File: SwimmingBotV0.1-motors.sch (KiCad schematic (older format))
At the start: 40 parts, among them P6 FIN1, P7 FIN2, P8 MOT1, P9 MOT2, Q10 PMV45EN2, Q11 PMV45EN2, Q12 PMV45EN2, Q13 PMV45EN2, Q14 PMV45EN2, Q15 PMV45EN2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

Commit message: woohoo getting there
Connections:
- net A1: now also P8.3 (P3); no longer P8.1 (P1)
- net A2: now also P9.3 (P3); no longer P9.1 (P1)
- net C1: now also P8.1 (P1); no longer P8.3 (P3)
- net C2: now also P9.1 (P1); no longer P9.3 (P3)
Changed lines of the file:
@@
 $Descr A4 11693 8268
 encoding utf-8
-Sheet 6 8
+Sheet 4 8
 Title ""
 Date ""
@@
 Wire Wire Line
 	8600 1500 8400 1500
-Text Label 8400 750  0    60   ~ 0
+Text Label 8400 950  0    60   ~ 0
 A1
 Text Label 8400 850  0    60   ~ 0
 B1
-Text Label 8400 950  0    60   ~ 0
+Text Label 8400 750  0    60   ~ 0
 C1
-Text Label 8400 1500 0    60   ~ 0
+Text Label 8400 1300 0    60   ~ 0
 C2
 Text Label 8400 1400 0    60   ~ 0
 B2
-Text Label 8400 1300 0    60   ~ 0
+Text Label 8400 1500 0    60   ~ 0
 A2
 Text Label 7100 5400 1    60   ~ 0

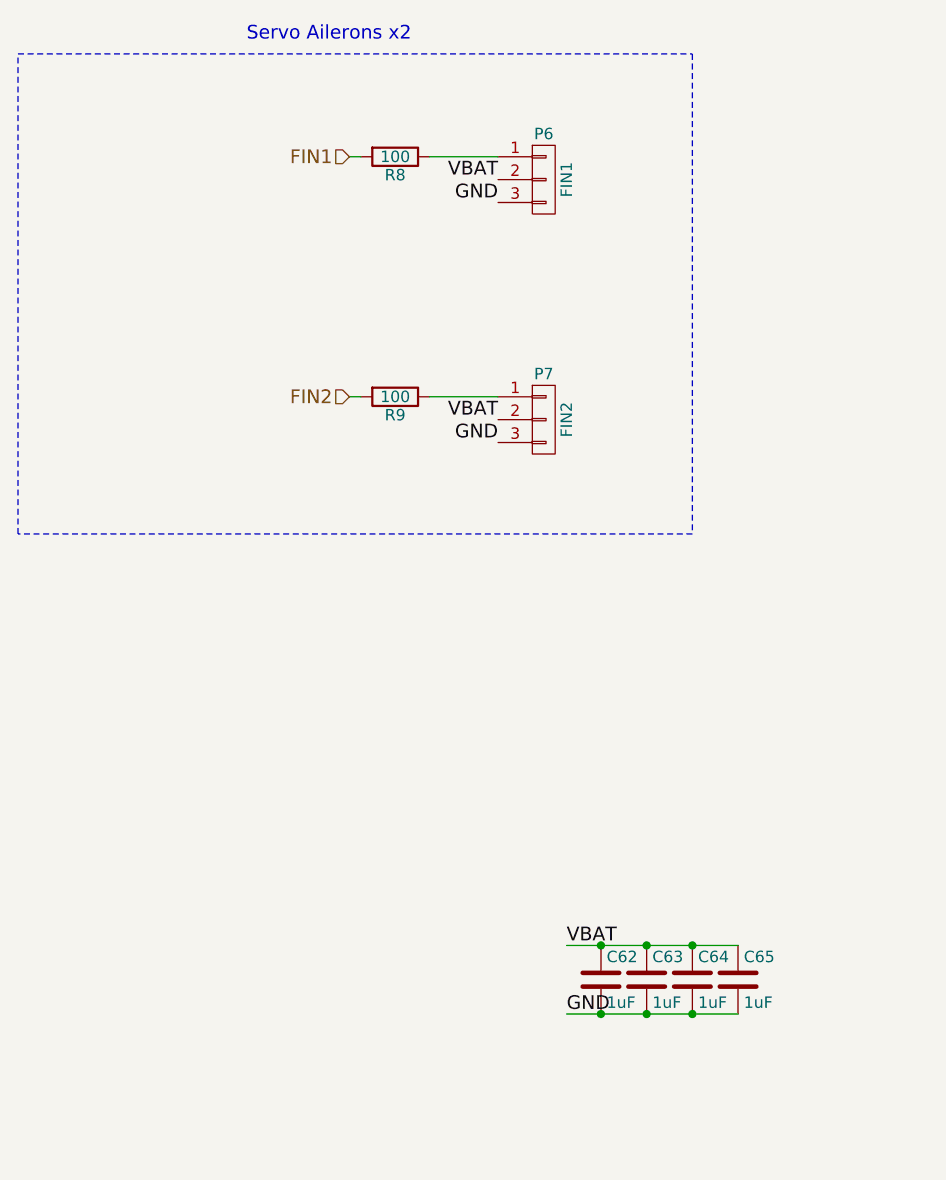
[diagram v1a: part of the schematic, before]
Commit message: potentially done with parts removal and reselection, on to pcb layout
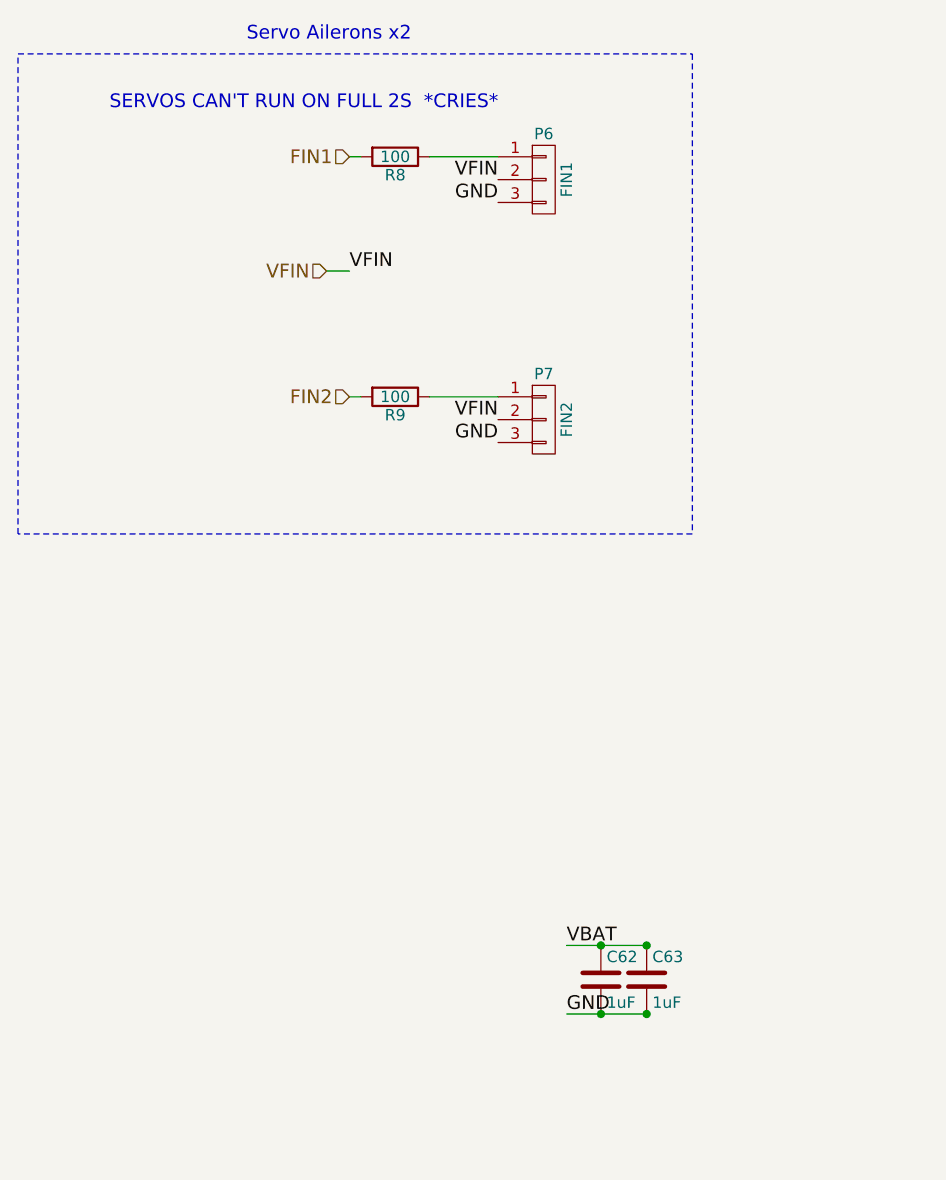
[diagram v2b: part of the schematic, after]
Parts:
- removed C64, C65: 1uF, Capacitors_SMD:C_0402, symbol C
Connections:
- net VBAT: no longer P6.2 (P2), P7.2 (P2)
- new net VFIN: P6.2 (P2), P7.2 (P2)
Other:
- note added: "SERVOS CAN'T RUN ON FULL 2S *CRIES*"
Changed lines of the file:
@@
 Wire Notes Line
 	750  2800 750  700
-Text Label 2850 1250 2    60   ~ 0
-VBAT
 Text Label 2850 2300 2    60   ~ 0
-VBAT
+VFIN
 Text Label 2850 1350 2    60   ~ 0
 GND
@@
 	1    0    0    -1
 $EndComp
-$Comp
-L C C64
-U 1 1 574E8796
-P 3700 4750
-F 0 "C64" H 3725 4850 50  0000 L CNN
-F 1 "1uF" H 3725 4650 50  0000 L CNN
-F 2 "Capacitors_SMD:C_0402" H 3738 4600 50  0001 C CNN
-F 3 "" H 3700 4750 50  0000 C CNN
-	1    3700 4750
-	1    0    0    -1
-$EndComp
-$Comp
-L C C65
-U 1 1 574E881F
-P 3900 4750
-F 0 "C65" H 3925 4850 50  0000 L CNN
-F 1 "1uF" H 3925 4650 50  0000 L CNN
-F 2 "Capacitors_SMD:C_0402" H 3938 4600 50  0001 C CNN
-F 3 "" H 3900 4750 50  0000 C CNN
-	1    3900 4750
-	1    0    0    -1
-$EndComp
-Wire Wire Line
-	3150 4600 3900 4600
-Connection ~ 3700 4600
 Connection ~ 3500 4600
-Wire Wire Line
-	3150 4900 3900 4900
 Connection ~ 3500 4900
-Connection ~ 3700 4900
 Connection ~ 3300 4600
 Connection ~ 3300 4900
@@
 Text Label 3150 4900 0    60   ~ 0
 GND
+Text Notes 1150 950  0    60   ~ 0
+SERVOS CAN'T RUN ON FULL 2S  *CRIES*
+Text Label 2850 1250 2    60   ~ 0
+VFIN
+Text HLabel 2100 1650 0    60   Input ~ 0
+VFIN
+Wire Wire Line
+	2100 1650 2200 1650
+Text Label 2200 1650 0    60   ~ 0
+VFIN
+Wire Wire Line
+	3150 4600 3500 4600
+Wire Wire Line
+	3150 4900 3500 4900
 $EndSCHEMATC

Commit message: pcb started in earnest, footprint changes in schematics, about to rename v0.2 boardfile to v0.1, kicad needs the same filename to have backrefs for net highlighting
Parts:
- P6, P7, P8, P9: footprint Custom_Footprints:PICO-EZMATE-3 -> Pin_Headers:Pin_Header_Straight_1x03_Pitch2.00mm
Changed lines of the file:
@@
 F 0 "P8" H 8800 1050 50  0000 C CNN
 F 1 "MOT1" V 8900 850 50  0000 C CNN
-F 2 "Custom_Footprints:PICO-EZMATE-3" H 8800 850 50  0001 C CNN
+F 2 "Pin_Headers:Pin_Header_Straight_1x03_Pitch2.00mm" H 8800 850 50  0001 C CNN
 F 3 "" H 8800 850 50  0000 C CNN
 	1    8800 850
@@
 F 0 "P9" H 8800 1600 50  0000 C CNN
 F 1 "MOT2" V 8900 1400 50  0000 C CNN
-F 2 "Custom_Footprints:PICO-EZMATE-3" H 8800 1400 50  0001 C CNN
+F 2 "Pin_Headers:Pin_Header_Straight_1x03_Pitch2.00mm" H 8800 1400 50  0001 C CNN
 F 3 "" H 8800 1400 50  0000 C CNN
 	1    8800 1400
@@
 F 0 "P6" H 3050 1450 50  0000 C CNN
 F 1 "FIN1" V 3150 1250 50  0000 C CNN
-F 2 "Custom_Footprints:PICO-EZMATE-3" H 3050 1250 50  0001 C CNN
+F 2 "Pin_Headers:Pin_Header_Straight_1x03_Pitch2.00mm" H 3050 1250 50  0001 C CNN
 F 3 "" H 3050 1250 50  0000 C CNN
 	1    3050 1250
@@
 F 0 "P7" H 3050 2500 50  0000 C CNN
 F 1 "FIN2" V 3150 2300 50  0000 C CNN
-F 2 "Custom_Footprints:PICO-EZMATE-3" H 3050 2300 50  0001 C CNN
+F 2 "Pin_Headers:Pin_Header_Straight_1x03_Pitch2.00mm" H 3050 2300 50  0001 C CNN
 F 3 "" H 3050 2300 50  0000 C CNN
 	1    3050 2300
